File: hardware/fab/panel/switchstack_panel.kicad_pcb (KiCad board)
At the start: 2 copper layers, 178.4 x 64.4 mm, 234 parts

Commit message: Klinke nach 6 Uhr, ToF bleibt 12 Uhr - USB-C weicht nach oben aus
Beide Durchbrueche der Frontplatte sassen im oberen Steg. Der ToF gehoert
dorthin - er soll nach vorn und in die Fensteroeffnung schauen, nicht auf die
Fensterbank. Der Steckplatz gehoert nach unten, sonst haengt das Sternkabel
quer ueber der Anzeige.

Frontplatte
-----------
jack_x/jack_y von (-4,0 / +22,5) auf (0 / -22,5). Die Stegbreite bleibt: das
Ringskizze schneidet beide Rechtecke symmetrisch, alle vier Stege sind ohnehin
17 mm breit. Der Selbsttest pruefte fest verdrahtet den 90-Grad-Steg auf zwei
Durchbrueche; er sortiert die Loecher jetzt selbst nach Steg und prueft beide.
Materialbahnen: oben 11,25 und 1,25 mm, unten 5,70 und 5,70 mm. Selbsttest
BESTANDEN, STEP/STL neu erzeugt.

Top-Layout
----------
Die Klinke stand auf 6 Uhr im Weg - dort sass die USB-C-Buchse. Neue Ordnung:

  12 Uhr   ToF bei x=+5, USB-C links daneben (Mitte x=-3,875)
   6 Uhr   Klinkenbuchse mittig
   innen   J7 (Reserve-UART, DNP) nach rechts neben den Displayanschluss

Zur USB-C-Lage: Das Fenster zwischen dem ToF und dem Taster auf 123 Grad ist
knapp 12 mm breit. Tangential gedreht waechst die BBOX des Verbinders auf
12,2 mm - passt nicht. Achsparallel sind es 8,95 mm, es bleiben je 1,5 mm Luft.
Das Steckgesicht liegt dabei leicht innerhalb der Kontur; der Stecker ragt ueber
die 1 mm duenne Platine hinweg, das kostet nichts, waehrend Kupfer ueber der
Kante an die Dosenwand stiesse.

J7 musste weichen und findet automatisch keinen Platz: Als THT-Teil braucht er
beide Seiten frei, und die Vorderseite innerhalb r21 gehoert dem Displaymodul.
Deshalb wieder fest platziert, kurz zu J3, aus dem sein UART kommt.

Ergebnis: Platzierung kollisionsfrei, Randabstandsverletzungen 11 -> 1. Die
verbliebene ist der Platzhalter-Footprint der Klinke (Punkt 30): 14,4 mm lang
mit dem Bund in der Mitte, bei r = 22,5 steht das hintere Ende 3,3 mm ueber die
Kante. Punkt 30 nennt jetzt das Zielmass - das reale 2,5-mm-Teil muss in einen
Ring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
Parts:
- T_C3, T_R1: moved to B.Cu
- moved T_J6 56.7 mm to (57.0, 28.3), turned to 180 degrees
- moved T_R2 43.7 mm to (59.7, -20.1)
- moved T_J1 41.8 mm to (56.1, -16.0)
- moved T_C4 39.8 mm to (62.4, -19.0), turned to 0 degrees
- moved T_R1 39.7 mm to (59.5, -16.8), turned to 90 degrees
- moved T_U1 34.9 mm to (57.6, -12.8)
- moved T_C3 33.6 mm to (59.1, -9.67)
- moved T_Q1 31.9 mm to (53.2, -12.5), turned to 0 degrees
- moved T_R4 29.7 mm to (54.8, -5.71)
- moved T_Q2 29.7 mm to (54.0, -8.60)
- moved T_R3 28.7 mm to (50.1, -11.0), turned to 90 degrees
- moved T_C1 27.5 mm to (60.9, -12.3), turned to 90 degrees
- moved T_J7 14.0 mm to (61.6, 12.0), turned to 90 degrees
- turned T_R5 to 90 degrees

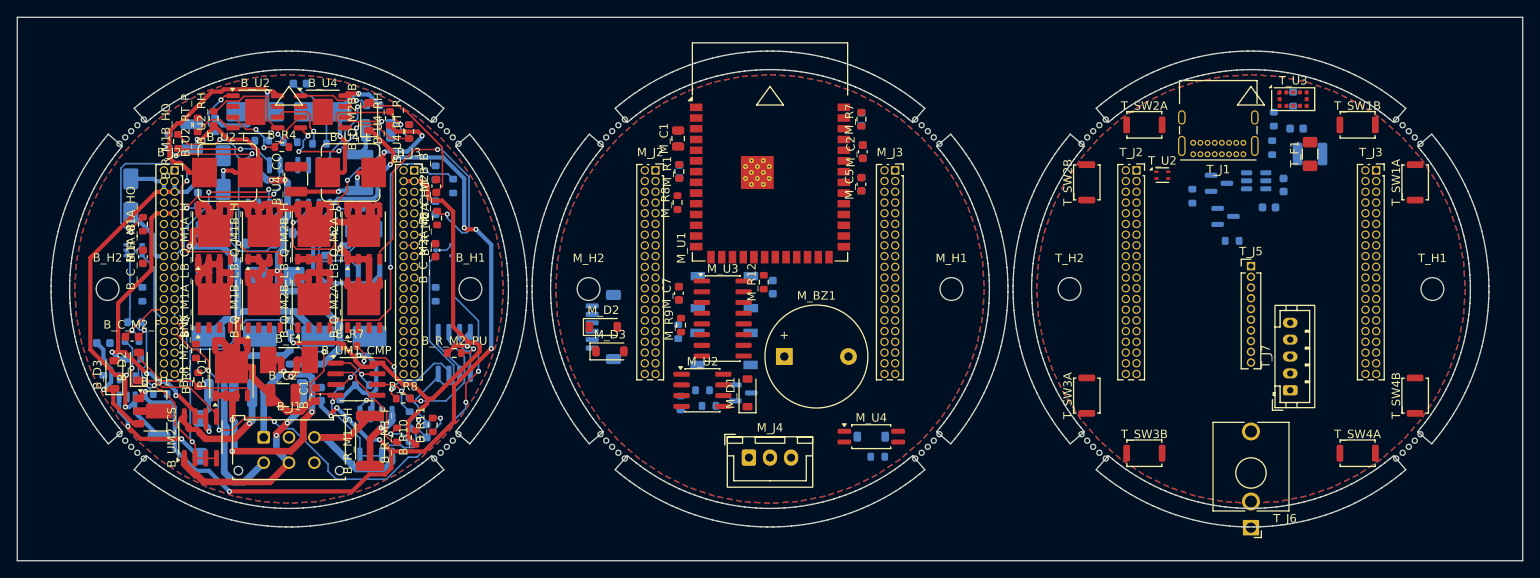
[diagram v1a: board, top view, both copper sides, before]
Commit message: Stehende USB-C-Buchse, Nutzen mit gemischter Geometrie - Top ist DRC-sauber
USB-C (Punkt 45)
----------------
Gewaehlt: G-Switch GT-USB-7051x, vertikal SMT, 22 Pads (A- und B-Reihe
vollstaendig, also steckrichtungsunabhaengig), Footprint 9,94 x 6,40 mm,
LCSC C2843970. Sie sitzt mittig oben, zeigt nach vorn und liegt unter der
Zentralscheibe - erreichbar erst nach deren Abnahme, so wie es Punkt 45
verlangt.

Der Nebeneffekt ist der eigentliche Gewinn: Die 28 clearance-Meldungen, die das
Top-Board seit dem ersten Layout begleitet haben, sind verschwunden. Sie waren
nie ein Layoutfehler, sondern die zu eng gerasterten Pads der liegenden GCT
USB4085 gegen unsere 0,15-mm-Vorgabe. Das Top-Board meldet jetzt KEINEN
DRC-Fehler mehr - nur noch drei bewusste Randverletzungen (zwei davon sind die
NPTH-Loecher der Buchse gegen ihre eigenen Pads, eine der Klinken-Platzhalter).

Der Waiver-Mechanismus in gen_layouts.py war dafuer zu grob: Er hat nur auf das
Zeilenende geprueft. Jetzt wird nur gewaivert, wenn ALLE in der Meldung
genannten Bauteile in der Ausnahmeliste stehen - sonst verschluckt ein Waiver
fuer J1 auch eine echte Kollision J1 gegen U3.

Fertigungsnutzen
----------------
gen_panel.py beherrscht gemischte Geometrie: zwei Kreise Oe52 und ein
abgerundetes Quadrat 47 x 47. Das Quadrat bekommt seine Fraesfuge als
Parallelkurve der Kontur, mit vier Stegen - je einer pro Kante, um 10 mm aus der
Mitte versetzt, weil dort entweder eine Befestigungsbohrung oder der
ueberstehende Klinken-Platzhalter sitzt. 173,4 x 64,4 mm = 112 cm2.

Zwei Fehler dabei gefunden und behoben: Die geschlossene Konturliste endete auf
ihrem eigenen Anfangspunkt - beim Umlauf entstand ein Segment der Laenge null,
und KiCad meldete die ganze Kontur als ungueltig. Und die Seitennamen der Stege
sind KiCad-Koordinaten mit y nach unten; die erste Fassung setzte den Steg
deshalb genau auf die Klinke.

Der DRC des Nutzens ist wieder deckungsgleich mit der Summe der Einzelboards.

Co-Authored-By: Claude Opus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
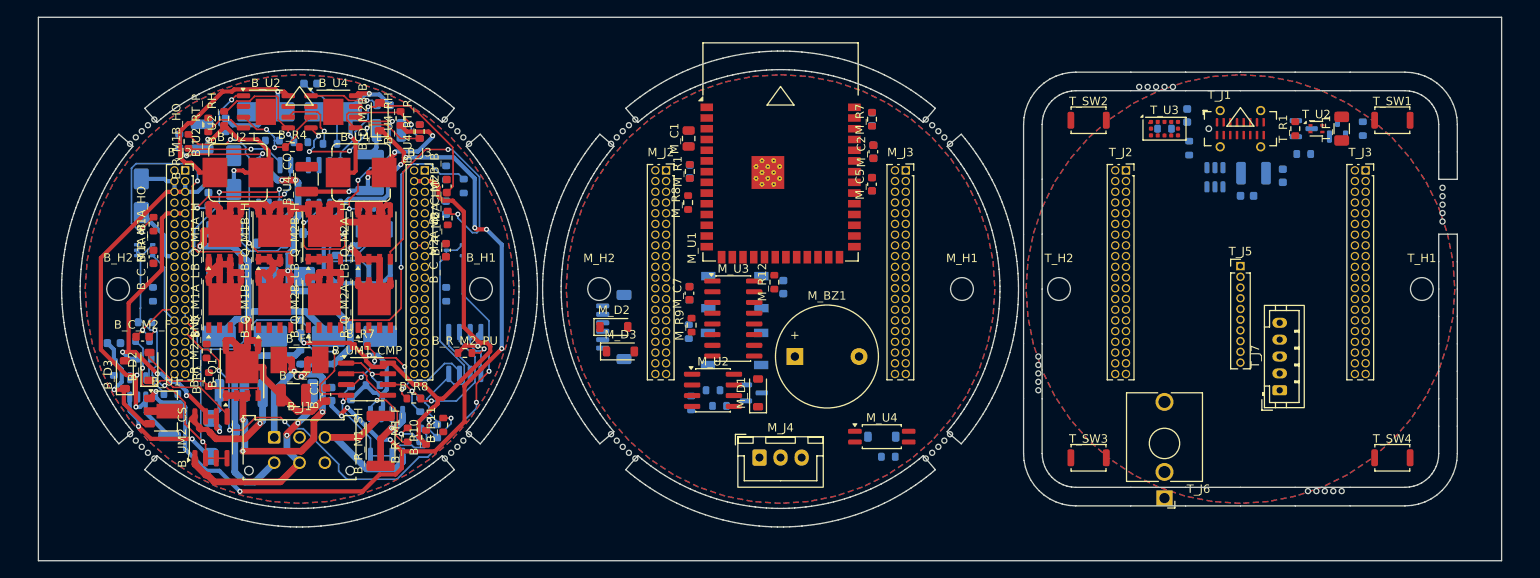
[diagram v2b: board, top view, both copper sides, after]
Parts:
- removed the MB at (-39.8, -20.1)
- removed the MB at (77.1, 17.2)
- removed the MB at (-38.3, 18.7)
- removed the MB at (39.8, -20.1)
- removed the MB at (74.2, -20.1)
- removed the MB at (-38.3, -18.7)
- removed the MB at (20.1, -17.2)
- removed the MB at (20.1, 17.2)
- removed the MB at (-18.7, -18.7)
- removed the MB at (-76.4, 18.0)
- removed the MB at (-77.1, -17.2)
- removed the MB at (39.8, 20.1)
- removed the MB at (18.0, -19.4)
- removed the MB at (-75.0, -19.4)
- removed the MB at (38.3, -18.7)
- removed the MB at (-37.6, 18.0)
- removed the MB at (18.0, 19.4)
- removed the MB at (-18.7, 18.7)
- removed the MB at (75.7, 18.7)
- removed the MB at (19.4, 18.0)
- removed the MB at (-37.6, -18.0)
- removed the MB at (-19.4, -18.0)
- removed the MB at (-74.2, -20.1)
- removed the MB at (-36.9, -17.2)
- removed the MB at (-20.1, -17.2)
- removed the MB at (-39.8, 20.1)
- removed the MB at (17.2, 20.1)
- removed the MB at (-18.0, 19.4)
- removed the MB at (-19.4, 18.0)
- removed the MB at (75.0, 19.4)
- removed the MB at (19.4, -18.0)
- removed the MB at (18.7, 18.7)
- removed the MB at (-17.2, 20.1)
- removed the MB at (-77.1, 17.2)
- removed the MB at (-17.2, -20.1)
- removed the MB at (75.7, -18.7)
- removed the MB at (76.4, 18.0)
- removed the MB at (39.0, -19.4)
- removed the MB at (-75.7, 18.7)
- removed the MB at (39.0, 19.4)
- removed the MB at (-20.1, 17.2)
- removed the MB at (-39.0, -19.4)
- removed the MB at (37.6, 18.0)
- removed the MB at (-75.0, 19.4)
- removed the MB at (-36.9, 17.2)
- removed the MB at (76.4, -18.0)
- removed the MB at (-39.0, 19.4)
- removed the MB at (36.9, -17.2)
- removed the MB at (-76.4, -18.0)
- removed the MB at (36.9, 17.2)
- removed the MB at (38.3, 18.7)
- removed the MB at (17.2, -20.1)
- removed the MB at (-18.0, -19.4)
- removed the MB at (37.6, -18.0)
- removed the MB at (74.2, 20.1)
- removed the MB at (75.0, -19.4)
- removed the MB at (-75.7, -18.7)
- removed the MB at (18.7, -18.7)
- removed the MB at (77.1, -17.2)
- removed the MB at (-74.2, 20.1)
- removed T_SW1A, T_SW1B: BTN1, SW_Push_SPST_NO_Alps_SKRK
- removed T_SW2A, T_SW2B: BTN2, SW_Push_SPST_NO_Alps_SKRK
- removed T_SW3A, T_SW3B: BTN3, SW_Push_SPST_NO_Alps_SKRK
- removed T_SW4A, T_SW4B: BTN4, SW_Push_SPST_NO_Alps_SKRK
- added MB: , , F.Cu at (-18.8, -17.2)
- added MB: , , F.Cu at (31.8, 11.0)
- added MB: , , F.Cu at (79.7, -10.0)
- added MB: , , F.Cu at (-18.8, 17.2)
- added MB: , , F.Cu at (20.0, 18.7)
- added MB: , , F.Cu at (47.8, -23.9)
- added MB: , , F.Cu at (-38.5, 20.1)
- added MB: , , F.Cu at (79.7, -11.0)
- added MB: , , F.Cu at (20.0, -18.7)
- added MB: , , F.Cu at (-36.3, -18.0)
- added MB: , , F.Cu at (-75.8, 17.2)
- added MB: , , F.Cu at (-75.2, 18.0)
- added MB: , , F.Cu at (-73.7, 19.4)
- added MB: , , F.Cu at (31.8, 12.0)
- added MB: , , F.Cu at (19.2, -19.4)
- added MB: , , F.Cu at (18.5, -20.1)
- added MB: , , F.Cu at (79.7, -8.00)
- added MB: , , F.Cu at (31.8, 9.00)
- added MB: , , F.Cu at (-75.8, -17.2)
- added MB: , , F.Cu at (-16.7, -19.4)
- added MB: , , F.Cu at (-37.0, -18.7)
- added MB: , , F.Cu at (-74.5, 18.7)
- added MB: , , F.Cu at (21.3, -17.2)
- added MB: , , F.Cu at (-17.5, 18.7)
- added MB: , , F.Cu at (-73.0, 20.1)
- added MB: , , F.Cu at (-36.3, 18.0)
- added MB: , , F.Cu at (-74.5, -18.7)
- added MB: , , F.Cu at (31.8, 10.0)
- added MB: , , F.Cu at (20.7, -18.0)
- added MB: , , F.Cu at (-37.0, 18.7)
- added MB: , , F.Cu at (18.5, 20.1)
- added MB: , , F.Cu at (79.7, -12.0)
- added MB: , , F.Cu at (-16.0, -20.1)
- added MB: , , F.Cu at (43.8, -23.9)
- added MB: , , F.Cu at (67.8, 23.9)
- added MB: , , F.Cu at (-37.8, 19.4)
- added MB: , , F.Cu at (-16.7, 19.4)
- added MB: , , F.Cu at (-73.7, -19.4)
- added MB: , , F.Cu at (-17.5, -18.7)
- added MB: , , F.Cu at (-35.7, -17.2)
- added MB: , , F.Cu at (65.8, 23.9)
- added MB: , , F.Cu at (45.8, -23.9)
- added MB: , , F.Cu at (-18.2, -18.0)
- added MB: , , F.Cu at (63.8, 23.9)
- added MB: , , F.Cu at (66.8, 23.9)
- added MB: , , F.Cu at (31.8, 8.00)
- added MB: , , F.Cu at (-16.0, 20.1)
- added MB: , , F.Cu at (19.2, 19.4)
- added MB: , , F.Cu at (-18.2, 18.0)
- added MB: , , F.Cu at (64.8, 23.9)
- added MB: , , F.Cu at (-35.7, 17.2)
- added MB: , , F.Cu at (46.8, -23.9)
- added MB: , , F.Cu at (44.8, -23.9)
- added MB: , , F.Cu at (-75.2, -18.0)
- added MB: , , F.Cu at (20.7, 18.0)
- added MB: , , F.Cu at (-37.8, -19.4)
- added MB: , , F.Cu at (79.7, -9.00)
- added MB: , , F.Cu at (-73.0, -20.1)
- added MB: , , F.Cu at (-38.5, -20.1)
- added MB: , , F.Cu at (21.3, 17.2)
- added T_SW1: BTN1, SW_Push_SPST_NO_Alps_SKRK, F.Cu at (73.8, -20.0)
- added T_SW2: BTN2, SW_Push_SPST_NO_Alps_SKRK, F.Cu at (37.8, -20.0)
- added T_SW3: BTN3, SW_Push_SPST_NO_Alps_SKRK, F.Cu at (37.8, 20.0)
- added T_SW4: BTN4, SW_Push_SPST_NO_Alps_SKRK, F.Cu at (73.8, 20.0)
- T_J1: footprint USB_C_Receptacle_GCT_USB4085 -> USB_C_Receptacle_G-Switch_GT-USB-7051x
- T_J5: value ST77916 QSPI -> ST7789 240x280
- T_R1: moved to F.Cu
- moved T_R4 20.4 mm to (70.2, -19.0), turned to 90 degrees
- moved T_U2 19.1 mm to (64.8, -19.0)
- moved T_Q2 16.9 mm to (67.2, -19.0), turned to 90 degrees
- moved T_R5 15.6 mm to (46.8, -19.0), turned to 0 degrees
- moved T_U3 15.6 mm to (46.8, -19.0)
- moved T_R3 14.1 mm to (63.2, -16.0), turned to 0 degrees
- moved T_C1 14.1 mm to (49.4, -20.6)
- moved T_Q1 11.9 mm to (63.2, -19.0)
- moved T_J6 10.8 mm to (46.8, 24.8)
- moved T_R2 10.6 mm to (49.7, -16.7)
- moved T_C4 9.90 mm to (56.5, -11.0)
- moved T_C2 7.08 mm to (57.3, -13.7)
- moved T_U1 4.91 mm to (52.7, -13.2), turned to 90 degrees
- moved T_F1 4.80 mm to (67.8, -19.0)
- moved T_C3 4.10 mm to (60.8, -13.4), turned to 90 degrees
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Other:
- board size 178.4 x 64.4 mm -> 173.4 x 64.4 mm

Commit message: Blockierstrom gemessen: 1,6 A statt 25 A - Auslegung neu gerechnet
Am 17.08.2026 mit blockiertem Abtrieb gemessen: 1,6 A bei 24 V, Netzteil mit
5 A Reserve, also keine Strombegrenzung. Daraus R_Anker = 15 Ohm. Die Messung
vom Vortag (0,116 A bei 2 V, 17,2 Ohm) bestaetigt das aus einem zwoelffach
anderen Betriebspunkt - die Zwischenbewertung "unbrauchbar" war falsch und ist
zurueckgenommen. Aufgeloest ist damit auch der Widerspruch zum Typenschild:
24 V an 15 Ohm ergeben maximal 38 W, die 100 W sind die Netzteilempfehlung der
Anlage, nicht die Aufnahme eines Motors.

GEAENDERTE WERTE - kein Layout betroffen:

  Shunt R_M1_SH/R_M2_SH   1 mOhm -> 5 mOhm    (gleicher Footprint)
  Trip-Teiler R8          40k2   -> 30k9      (+/-22 A -> +/-4,0 A)
  Sicherung F1            15 A   -> 6,3 A traege
  Firmware-Skalierung     20 A/V -> 4 A/V

Der Shunt wird groesser, nicht kleiner: Er bestimmt nicht die Belastbarkeit,
sondern die Aufloesung. Am 1-mOhm-Shunt lagen zwischen Fahrt und Anschlag nur
30-65 mV, in der Groessenordnung des ADC-Rauschens. Mit 5 mOhm sind es
150-325 mV bei 0,25 V/A und +/-6,6 A Messbereich; die Verlustleistung betraegt
bei 2 A ganze 20 mW.

Die Trip-Schwelle muss UEBER dem Blockierstrom liegen, weil der Anschlag ohne
Endschalter ein normaler Betriebszustand ist - der Laden faehrt bei jeder Fahrt
kurz dagegen. 4,0 A gibt Faktor 2,5 Reserve, ein echter Kurzschluss liegt
Groessenordnungen darueber.

FEHLER IN DER FIRMWARE MITGEFUNDEN: Der Nullpunkt des INA240 wurde nirgends
abgezogen. Der Sensor haette im Stillstand 6,6 A gemeldet statt 0 A. Jetzt
Betragsbildung um einen einstellbaren Nullpunkt (Vorgabe 1,65 V), damit auch
die Richtungsumkehr am Inline-Shunt kein Vorzeichen mehr erzeugt.

WAS DIE MESSUNG ERLEDIGT: Punkt 1 (Blockierstrom), Punkt 2 (Steckverbinder -
Micro-Fit 3.0 reicht, Mini-Fit Jr. nicht noetig) und die Verschaerfung von
Punkt 3. Der Summenstrom faellt von 9 A auf 3,9 A im unguenstigsten Fall.
Ein Anlaufstrom ueber dem Blockierstrom existier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
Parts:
- B_R8: value 40k2 -> 30k9
- B_R_M1_SH, B_R_M2_SH: value 1m0 1W -> 5m0 1W
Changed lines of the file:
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@@
 			)
 		)
-		(property "Value" "1m0 1W"
+		(property "Value" "5m0 1W"
 			(at 0 2.62 90)
 			(layer "F.Fab")
@@
 			)
 		)
-		(property "Value" "40k2"
+		(property "Value" "30k9"
 			(at 0 1.43 0)
 			(layer "F.Fab")
@@
 			)
 		)
-		(property "Value" "1m0 1W"
+		(property "Value" "5m0 1W"
 			(at 0 -2.62 180)
 			(layer "B.Fab")

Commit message: Reserve nachgerechnet: Wind, Messfehler - und ein Fehler am Komparator
Nachgegangen der Frage, wie sicher der gemessene Blockierstrom ist und was bei
Wind passiert. Drei Ergebnisse, docs/11 Abschnitt 6 neu.

1) DER BLOCKIERSTROM IST EINE HARTE OBERGRENZE, keine Lastannahme. Bei
   blockiertem Laeufer ist die Gegenspannung null, also I = U/R. Ein Drehmoment
   kommt in der Gleichung nicht vor - Wind kann den Motor nur langsamer machen,
   und langsamer heisst naeher an 1,6 A, nie darueber. Ueberschritten wird die
   Grenze nur beim Umpolen eines noch drehenden Motors (bis 3,2 A), und dagegen
   stehen 300 ms Stoppause und die Selbsthemmung des Schneckengetriebes.

   Der Trip liegt mit 4,4 A ueber allen drei denkbaren Faellen.

2) TRIP-TEILER BLEIBT BEI 40k2 statt der gestern eingesetzten 30k9. Der
   groessere Shunt nimmt die Schwelle von allein von 22 A auf 4,4 A mit - ein
   Bauteil weniger geaendert, und die zusaetzliche Reserve kostet nichts, weil
   zwischen 4 und 5 A auf dieser Platine ohnehin nichts gefaehrdet ist. Damit
   traegt die Auslegung einen Messfehler von Faktor 2,5.

   Gegenprobe fuer Faktor 2 (3,2 A statt 1,6 A) in Abschnitt 6.2: Es reagieren
   genau zwei Positionen, und die Sicherung ist dabei kein Risiko, sondern der
   Melder - sie fliegt beim ersten beidseitigen Anschlag, harmlos und sofort
   sichtbar.

   Billige dritte Bestaetigung: M6 mit dem Multimeter ist bei 15 Ohm endlich
   brauchbar (Zuleitungen unter 3 % statt der Haelfte). Erwartet 14-17 Ohm,
   zwei Minuten, kein Blockieren.

3) WIND IST EIN MECHANISCHES PROBLEM. Ueberschlag fuer 0,84 m2 Flaeche: Ab
   etwa 40 km/h uebersteigt das Windmoment am Band die 25 Nm des Motors, bei
   90 km/h steht das Fuenffache dagegen. Elektrisch aendert das nichts, die
   Endlagenerkennung bricht aber in beide Richtungen: Gegenwind sieht aus wie
   ein Anschlag, Rueckenwind schlaegt den Fluegel bei NIEDRIGEREM Strom als
   normal gegen den Anschlag. Punkt 58 mit drei Gegenmassnahmen, davon die
   w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
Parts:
- B_R8: value 30k9 -> 40k2
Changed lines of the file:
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@@
 			)
 		)
-		(property "Value" "30k9"
+		(property "Value" "40k2"
 			(at 0 1.43 0)
 			(layer "F.Fab")

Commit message: TLV3702 statt LM393; Auslegung auf den kleinsten gemessenen Wert (14 Ohm)
ZWEI SACHEN IN EINEM COMMIT, weil beide aus derselben Messreihe kommen.

1) M6 vollstaendig: 16,5 / 20 / 14 Ohm. Die Streuung ist der erwartete
   Buersteneffekt - je nach Laeuferstellung liegen unterschiedlich viele
   Lamellen im Strompfad. Fuer die Auslegung zaehlt das Minimum, und das sind
   jetzt 14 Ohm statt der 15,0 Ohm aus M3. Damit steigt der Blockierstrom von
   1,6 auf 1,7 A, der Summenpfad von 3,9 auf 4,1 A und die Maximalaufnahme je
   Motor von 38 auf 41 W.

   Kein Bauteil aendert sich: Ausgelegt war ohnehin auf 2 A, der Trip liegt bei
   4,4 A (Faktor 2,6), die Sicherung bei 6,3 A. Die Zahlen sind nur ueberall
   konsistent nachgezogen.

   Damit ist der Blockierstrom dreifach unabhaengig bestaetigt - 2 V, 24 V
   blockiert, Multimeter - und der Faktor-2-Irrtum ausgeschlossen.

2) Punkt 57 geloest, und zwar OHNE die geroutete Platine anzufassen.

   Der Weg ueber 5V_SYS, den der Nutzer zunaechst gewaehlt hatte, scheiterte an
   der Geometrie: Das Netz liegt komplett auf der linken Boardhaelfte, die
   Komparatoren rechts - 27,3 bzw. 36,0 mm entfernt, zwei lange Bahnen ueber
   985 vorhandene Segmente. 12V_GATE waere mit 3-7 mm nah, ist aber die
   lauteste Schiene der Platine, und der Komparator hat keinen eigenen
   Abblockkondensator.

   Gewaehlt: TLV3702. Rail-to-Rail-Eingang, Open-Drain, SOIC-8 im
   Standard-Pinout eines dualen Komparators. Gleicher Footprint, gleiche Netze,
   keine Leiterbahn angefasst, DRC unveraendert (228 Meldungen, alle
   Bestueckungsdruck; 61 offene Verbindungen wie zuvor). Er bleibt an 3,3 V und
   damit auf derselben Schiene wie die INA240-Referenz, was die ratiometrische
   Kopplung der Trip-Schwelle erhaelt. Mit rund 5 us ist er langsamer als der
   LM393 - hier ein Vorteil, weil der Komparator das ungefilterte Sense-Signal
   sieht und an einem Latch haengt (Punkt 59).

   ACHTUNG fuer die Bestellung: KiCad 10 bringt kein TLV-Symbol mit, im
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
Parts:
- B_UM1_CMP, B_UM2_CMP: value LM393 -> TLV3702
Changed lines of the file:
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@@
 			)
 		)
-		(property "Value" "LM393"
+		(property "Value" "TLV3702"
 			(at 0 3.4 0)
 			(layer "F.Fab")
@@
 			)
 		)
-		(property "Value" "LM393"
+		(property "Value" "TLV3702"
 			(at 0 -3.4 270)
 			(layer "B.Fab")
